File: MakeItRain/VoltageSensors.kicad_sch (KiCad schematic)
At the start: 4 parts, among them IC5 OPA2340PA

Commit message: wip
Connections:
- no-connect marks 3 -> 0
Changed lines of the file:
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@@
   (junction (at 132.08 77.47) (diameter 0) (color 0 0 0 0)
   )
-  (no_connect (at 163.83 80.01))
-  (no_connect (at 163.83 85.09))
-  (no_connect (at 163.83 82.55))
   (wire (pts (xy 119.38 81.28) (xy 119.38 82.55))
     (stroke (width 0) (type default) (color 0 0 0 0))

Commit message: wip for input fix.
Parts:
- R21: renamed from R5; footprint Resistor_THT:R_Axial_DIN0207_L6.3mm_D2.5mm_P5.08mm_Vertical -> Resistor_THT:R_Axial_DIN0207_L6.3mm_D2.5mm_P2.54mm_Vertical
- R22: renamed from R8; footprint Resistor_THT:R_Axial_DIN0207_L6.3mm_D2.5mm_P5.08mm_Vertical -> Resistor_THT:R_Axial_DIN0207_L6.3mm_D2.5mm_P2.54mm_Vertical
- R23: renamed from R13; footprint Resistor_THT:R_Axial_DIN0207_L6.3mm_D2.5mm_P5.08mm_Vertical -> Resistor_THT:R_Axial_DIN0207_L6.3mm_D2.5mm_P2.54mm_Vertical
- renumbered IC5 to IC3
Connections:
- net D36: now reaches IC3.1 (OUTA), IC3.2 (-INA), R23.1
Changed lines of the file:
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@@
+    (stroke (width 0) (type default) (color 0 0 0 0))
+  )
+  (wire (pts (xy 128.27 72.39) (xy 128.27 77.47))
     (stroke (width 0) (type default) (color 0 0 0 0))
   )
@@
     (stroke (width 0) (type default) (color 0 0 0 0))
   )
+  (global_label "D34" (shape input) (at 180.34 81.28 0) (fields_autoplaced)
+    (effects (font (size 1.27 1.27)) (justify left))
+    (property "Intersheet References" "${INTERSHEET_REFS}" (id 0) (at 186.3532 81.2006 0)
+      (effects (font (size 1.27 1.27)) (justify left) hide)
+    )
+  )
+  (global_label "D36" (shape input) (at 128.27 72.39 180) (fields_autoplaced)
+    (effects (font (size 1.27 1.27)) (justify right))
+    (property "Intersheet References" "${INTERSHEET_REFS}" (id 0) (at 122.2568 72.3106 0)
+      (effects (font (size 1.27 1.27)) (justify right) hide)
+    )
+  )
   (symbol (lib_id "Device:R") (at 119.38 77.47 0) (unit 1)
     (in_bom yes) (on_board yes)
-    (property "Reference" "R5" (id 0) (at 121.158 76.3016 0)
+    (property "Reference" "R21" (id 0) (at 121.158 76.3016 0)
       (effects (font (size 1.27 1.27)) (justify left))
     )
@@
       (effects (font (size 1.27 1.27)) (justify left))
     )
-    (property "Footprint" "Resistor_THT:R_Axial_DIN0207_L6.3mm_D2.5mm_P5.08mm_Vertical" (id 2) (at 117.602 77.47 90)
+    (property "Footprint" "Resistor_THT:R_Axial_DIN0207_L6.3mm_D2.5mm_P2.54mm_Vertical" (id 2) (at 117.602 77.47 90)
       (effects (font (size 1.27 1.27)) hide)
     )
@@
   (symbol (lib_id "power:+VDC") (at 119.38 68.58 0) (unit 1)
     (in_bom yes) (on_board yes)
-    (property "Reference" "#PWR027" (id 0) (at 119.38 71.12 0)
+    (property "Reference" "#PWR039" (id 0) (at 119.38 71.12 0)
       (effects (font (size 1.27 1.27)) hide)
     )
@@
   (symbol (lib_id "Device:R") (at 132.08 73.66 0) (mirror x) (unit 1)
     (in_bom yes) (on_board yes)
-    (property "Reference" "R13" (id 0) (at 133.858 74.8284 0)
+    (property "Reference" "R23" (id 0) (at 133.858 74.8284 0)
       (effects (font (size 1.27 1.27)) (justify left))
     )
@@
       (effects (font (size 1.27 1.27)) (justify left))
     )
-    (property "Footprint" "Resistor_THT:R_Axial_DIN0207_L6.3mm_D2.5mm_P5.08mm_Vertical" (id 2) (at 130.302 73.66 90)
+    (property "Footprint" "Resistor_THT:R_Axial_DIN0207_L6.3mm_D2.5mm_P2.54mm_Vertical" (id 2) (at 130.302 73.66 90)
       (effects (font (size 1.27 1.27)) hide)
     )
@@
   (symbol (lib_id "power:GND") (at 132.08 66.04 0) (mirror x) (unit 1)
     (in_bom yes) (on_board yes)
-    (property "Reference" "#PWR035" (id 0) (at 132.08 59.69 0)
+    (property "Reference" "#PWR041" (id 0) (at 132.08 59.69 0)
       (effects (font (size 1.27 1.27)) hide)
     )
@@
   (symbol (lib_id "power:GND") (at 119.38 95.25 0) (unit 1)
     (in_bom yes) (on_board yes)
-    (property "Reference" "#PWR031" (id 0) (at 119.38 101.6 0)
+    (property "Reference" "#PWR040" (id 0) (at 119.38 101.6 0)
       (effects (font (size 1.27 1.27)) hide)
     )
@@
   (symbol (lib_id "Device:R") (at 119.38 87.63 0) (unit 1)
     (in_bom yes) (on_board yes)
-    (property "Reference" "R8" (id 0) (at 121.158 86.4616 0)
+    (property "Reference" "R22" (id 0) (at 121.158 86.4616 0)
       (effects (font (size 1.27 1.27)) (justify left))
     )
@@
       (effects (font (size 1.27 1.27)) (justify left))
     )
-    (property "Footprint" "Resistor_THT:R_Axial_DIN0207_L6.3mm_D2.5mm_P5.08mm_Vertical" (id 2) (at 117.602 87.63 90)
+    (property "Footprint" "Resistor_THT:R_Axial_DIN0207_L6.3mm_D2.5mm_P2.54mm_Vertical" (id 2) (at 117.602 87.63 90)
       (effects (font (size 1.27 1.27)) hide)
     )
@@
   (symbol (lib_id "power:GND") (at 134.62 87.63 0) (unit 1)
     (in_bom yes) (on_board yes)
-    (property "Reference" "#PWR039" (id 0) (at 134.62 93.98 0)
+    (property "Reference" "#PWR042" (id 0) (at 134.62 93.98 0)
       (effects (font (size 1.27 1.27)) hide)
     )
@@
   (symbol (lib_id "SamacSys_Parts:OPA2340PA") (at 135.89 77.47 0) (unit 1)
     (in_bom yes) (on_board yes)
-    (property "Reference" "IC5" (id 0) (at 149.86 70.739 0))
+    (property "Reference" "IC3" (id 0) (at 149.86 70.739 0))
     (property "Value" "OPA2340PA" (id 1) (at 149.86 73.0504 0))
     (property "Footprint" "SamacSys_Parts:DIP794W53P254L959H508Q8N" (id 2) (at 160.02 74.93 0)

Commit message: wip for layout
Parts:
- added J4: Conn_01x03, Connector_PinHeader_2.54mm:PinHeader_1x03_P2.54mm_Vertical, symbol Connector_Generic:Conn_01x03
- added R?: 47k, Resistor_THT:R_Axial_DIN0207_L6.3mm_D2.5mm_P2.54mm_Vertical, symbol Device:R
- added RV1: 500k, Potentiometer_THT:Potentiometer_Bourns_3296W_Vertical, symbol Device:R_POT_US
- renumbered R21 to R23, R22 to R24, R23 to R25
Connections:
- net D34: now also IC3.6 (-INB), IC3.7 (OUTB), R?.1
- net GND: now also R?.2, RV1.3
- net at IC3.5 (+INB): now also J4.1 (Pin_1)
- new net: J4.2 (Pin_2), RV1.2
- new net: J4.3 (Pin_3), RV1.1
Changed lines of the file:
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@@
   (junction (at 132.08 77.47) (diameter 0) (color 0 0 0 0)
   )
+  (junction (at 172.72 80.01) (diameter 0) (color 0 0 0 0)
+  )
+  (junction (at 167.64 80.01) (diameter 0) (color 0 0 0 0)
+  )
   (wire (pts (xy 119.38 81.28) (xy 119.38 82.55))
     (stroke (width 0) (type default) (color 0 0 0 0))
   )
+  (wire (pts (xy 172.72 72.39) (xy 172.72 68.58))
+    (stroke (width 0) (type default) (color 0 0 0 0))
+  )
+  (wire (pts (xy 163.83 97.79) (xy 163.83 105.41))
+    (stroke (width 0) (type default) (color 0 0 0 0))
+  )
   (wire (pts (xy 134.62 85.09) (xy 135.89 85.09))
     (stroke (width 0) (type default) (color 0 0 0 0))
@@
     (stroke (width 0) (type default) (color 0 0 0 0))
   )
+  (wire (pts (xy 163.83 95.25) (xy 167.64 95.25))
+    (stroke (width 0) (type default) (color 0 0 0 0))
+  )
+  (wire (pts (xy 163.83 97.79) (xy 167.64 97.79))
+    (stroke (width 0) (type default) (color 0 0 0 0))
+  )
+  (wire (pts (xy 167.64 80.01) (xy 167.64 82.55))
+    (stroke (width 0) (type default) (color 0 0 0 0))
+  )
+  (wire (pts (xy 163.83 80.01) (xy 167.64 80.01))
+    (stroke (width 0) (type default) (color 0 0 0 0))
+  )
   (wire (pts (xy 163.83 77.47) (xy 167.64 77.47))
     (stroke (width 0) (type default) (color 0 0 0 0))
@@
     (stroke (width 0) (type default) (color 0 0 0 0))
   )
+  (wire (pts (xy 167.64 109.22) (xy 167.64 113.03))
+    (stroke (width 0) (type default) (color 0 0 0 0))
+  )
   (wire (pts (xy 128.27 72.39) (xy 128.27 77.47))
     (stroke (width 0) (type default) (color 0 0 0 0))
@@
     (stroke (width 0) (type default) (color 0 0 0 0))
   )
+  (wire (pts (xy 167.64 82.55) (xy 163.83 82.55))
+    (stroke (width 0) (type default) (color 0 0 0 0))
+  )
   (wire (pts (xy 134.62 87.63) (xy 134.62 85.09))
     (stroke (width 0) (type default) (color 0 0 0 0))
@@
     (stroke (width 0) (type default) (color 0 0 0 0))
   )
+  (wire (pts (xy 167.64 80.01) (xy 172.72 80.01))
+    (stroke (width 0) (type default) (color 0 0 0 0))
+  )
+  (wire (pts (xy 167.64 100.33) (xy 167.64 101.6))
+    (stroke (width 0) (type default) (color 0 0 0 0))
+  )
   (wire (pts (xy 119.38 82.55) (xy 119.38 83.82))
     (stroke (width 0) (type default) (color 0 0 0 0))
@@
     (stroke (width 0) (type default) (color 0 0 0 0))
   )
+  (wire (pts (xy 172.72 80.01) (xy 175.895 80.01))
+    (stroke (width 0) (type default) (color 0 0 0 0))
+  )
   (wire (pts (xy 132.08 69.85) (xy 132.08 66.04))
     (stroke (width 0) (type default) (color 0 0 0 0))
   )
-  (global_label "D34" (shape input) (at 180.34 81.28 0) (fields_autoplaced)
+  (wire (pts (xy 163.83 95.25) (xy 163.83 85.09))
+    (stroke (width 0) (type default) (color 0 0 0 0))
+  )
+  (global_label "D34" (shape input) (at 175.895 80.01 0) (fields_autoplaced)
     (effects (font (size 1.27 1.27)) (justify left))
-    (property "Intersheet References" "${INTERSHEET_REFS}" (id 0) (at 186.3532 81.2006 0)
+    (property "Intersheet References" "${INTERSHEET_REFS}" (id 0) (at 181.9082 79.9306 0)
       (effects (font (size 1.27 1.27)) (justify left) hide)
     )
@@
   (symbol (lib_id "Device:R") (at 119.38 77.47 0) (unit 1)
     (in_bom yes) (on_board yes)
-    (property "Reference" "R21" (id 0) (at 121.158 76.3016 0)
+    (property "Reference" "R23" (id 0) (at 121.158 76.3016 0)
       (effects (font (size 1.27 1.27)) (justify left))
     )
@@
   (symbol (lib_id "power:+VDC") (at 119.38 68.58 0) (unit 1)
     (in_bom yes) (on_board yes)
-    (property "Reference" "#PWR039" (id 0) (at 119.38 71.12 0)
+    (property "Reference" "#PWR042" (id 0) (at 119.38 71.12 0)
       (effects (font (size 1.27 1.27)) hide)
     )
@@
   (symbol (lib_id "Device:R") (at 132.08 73.66 0) (mirror x) (unit 1)
     (in_bom yes) (on_board yes)
-    (property "Reference" "R23" (id 0) (at 133.858 74.8284 0)
+    (property "Reference" "R25" (id 0) (at 133.858 74.8284 0)
       (effects (font (size 1.27 1.27)) (justify left))
     )
@@
   (symbol (lib_id "power:GND") (at 132.08 66.04 0) (mirror x) (unit 1)
     (in_bom yes) (on_board yes)
-    (property "Reference" "#PWR041" (id 0) (at 132.08 59.69 0)
+    (property "Reference" "#PWR044" (id 0) (at 132.08 59.69 0)
       (effects (font (size 1.27 1.27)) hide)
     )
@@
   (symbol (lib_id "power:GND") (at 119.38 95.25 0) (unit 1)
     (in_bom yes) (on_board yes)
-    (property "Reference" "#PWR040" (id 0) (at 119.38 101.6 0)
+    (property "Reference" "#PWR043" (id 0) (at 119.38 101.6 0)
       (effects (font (size 1.27 1.27)) hide)
     )
@@
     (pin "1")
   )
+  (symbol (lib_id "power:GND") (at 172.72 68.58 0) (mirror x) (unit 1)
+    (in_bom yes) (on_board yes)
+    (property "Reference" "#PWR?" (id 0) (at 172.72 62.23 0)
+      (effects (font (size 1.27 1.27)) hide)
+    )
+    (property "Value" "GND" (id 1) (at 172.847 64.1858 0))
+    (property "Footprint" "" (id 2) (at 172.72 68.58 0)
+      (effects (font (size 1.27 1.27)) hide)
+    )
+    (property "Datasheet" "" (id 3) (at 172.72 68.58 0)
+      (effects (font (size 1.27 1.27)) hide)
+    )
+    (pin "1")
+  )
+  (symbol (lib_id "Connector_Generic:Conn_01x03") (at 172.72 97.79 0) (unit 1)
+    (in_bom yes) (on_board yes) (fields_autoplaced)
+    (property "Reference" "J4" (id 0) (at 174.752 96.8815 0)
+      (effects (font (size 1.27 1.27)) (justify left))
+    )
+    (property "Value" "Conn_01x03" (id 1) (at 174.752 99.6566 0)
+      (effects (font (size 1.27 1.27)) (justify left))
+    )
+    (property "Footprint" "Connector_PinHeader_2.54mm:PinHeader_1x03_P2.54mm_Vertical" (id 2) (at 172.72 97.79 0)
+      (effects (font (size 1.27 1.27)) hide)
+    )
+    (property "Datasheet" "~" (id 3) (at 172.72 97.79 0)
+      (effects (font (size 1.27 1.27)) hide)
+    )
+    (pin "1")
+    (pin "2")
+    (pin "3")
+  )
+  (symbol (lib_id "Device:R_POT_US") (at 167.64 105.41 0) (mirror y) (unit 1)
+    (in_bom yes) (on_board yes)
+    (property "Reference" "RV1" (id 0) (at 169.3672 104.2416 0)
+      (effects (font (size 1.27 1.27)) (justify right))
+    )
+    (property "Value" "500k" (id 1) (at 169.3672 106.553 0)
+      (effects (font (size 1.27 1.27)) (justify right))
+    )
+    (property "Footprint" "Potentiometer_THT:Potentiometer_Bourns_3296W_Vertical" (id 2) (at 167.64 105.41 0)
+      (effects (font (size 1.27 1.27)) hide)
+    )
+    (property "Datasheet" "~" (id 3) (at 167.64 105.41 0)
+      (effects (font (size 1.27 1.27)) hide)
+    )
+    (pin "1")
+    (pin "2")
+    (pin "3")
+  )
   (symbol (lib_id "power:+3.3V") (at 167.64 74.93 0) (unit 1)
     (in_bom yes) (on_board yes)
-    (property "Reference" "#PWR043" (id 0) (at 167.64 78.74 0)
+    (property "Reference" "#PWR046" (id 0) (at 167.64 78.74 0)
       (effects (font (size 1.27 1.27)) hide)
     )
@@
   (symbol (lib_id "Device:R") (at 119.38 87.63 0) (unit 1)
     (in_bom yes) (on_board yes)
-    (property "Reference" "R22" (id 0) (at 121.158 86.4616 0)
+    (property "Reference" "R24" (id 0) (at 121.158 86.4616 0)
       (effects (font (size 1.27 1.27)) (justify left))
     )
@@
     (pin "2")
   )
+  (symbol (lib_id "Device:R") (at 172.72 76.2 0) (mirror x) (unit 1)
+    (in_bom yes) (on_board yes)
+    (property "Reference" "R?" (id 0) (at 174.498 77.3684 0)
+      (effects (font (size 1.27 1.27)) (justify left))
+    )
+    (property "Value" "47k" (id 1) (at 174.498 75.057 0)
+      (effects (font (size 1.27 1.27)) (justify left))
+    )
+    (property "Footprint" "Resistor_THT:R_Axial_DIN0207_L6.3mm_D2.5mm_P2.54mm_Vertical" (id 2) (at 170.942 76.2 90)
+      (effects (font (size 1.27 1.27)) hide)
+    )
+    (property "Datasheet" "~" (id 3) (at 172.72 76.2 0)
+      (effects (font (size 1.27 1.27)) hide)
+    )
+    (pin "1")
+    (pin "2")
+  )
+  (symbol (lib_id "power:GND") (at 167.64 113.03 0) (mirror y) (unit 1)
+    (in_bom yes) (on_board yes)
+    (property "Reference" "#PWR047" (id 0) (at 167.64 119.38 0)
+      (effects (font (size 1.27 1.27)) hide)
+    )
+    (property "Value" "GND" (id 1) (at 167.64 116.84 0))
+    (property "Footprint" "" (id 2) (at 167.64 113.03 0))
+    (property "Datasheet" "" (id 3) (at 167.64 113.03 0))
+    (pin "1")
+  )
   (symbol (lib_id "power:GND") (at 134.62 87.63 0) (unit 1)
     (in_bom yes) (on_board yes)
-    (property "Reference" "#PWR042" (id 0) (at 134.62 93.98 0)
-      (effects (font (size 1.27 1.27)) hide)
-    )
+    (property "Reference" "#PWR045" (id 0) (at 134.62 93.98 0)
+      (effects (font (size 1.27 1.27)) hide)
+    )

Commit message: pre routing
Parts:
- removed J4: Conn_01x03, Connector_PinHeader_2.54mm:PinHeader_1x03_P2.54mm_Vertical, symbol Connector_Generic:Conn_01x03
- added J4: Conn_01x01, Connector_PinHeader_2.54mm:PinHeader_1x01_P2.54mm_Vertical, symbol Connector_Generic:Conn_01x01
- gave numbers to parts that had none: 1
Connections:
- net at IC3.5 (+INB): now also RV1.2
- net AuxVoltage: now reaches RV1.1
- net AuxVoltage: now also J4.1 (Pin_1)
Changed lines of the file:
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@@
-    (stroke (width 0) (type default) (color 0 0 0 0))
-  )
-  (wire (pts (xy 163.83 97.79) (xy 163.83 105.41))
     (stroke (width 0) (type default) (color 0 0 0 0))
   )
@@
     (stroke (width 0) (type default) (color 0 0 0 0))
   )
-  (wire (pts (xy 163.83 95.25) (xy 167.64 95.25))
-    (stroke (width 0) (type default) (color 0 0 0 0))
-  )
-  (wire (pts (xy 163.83 97.79) (xy 167.64 97.79))
-    (stroke (width 0) (type default) (color 0 0 0 0))
-  )
   (wire (pts (xy 167.64 80.01) (xy 167.64 82.55))
     (stroke (width 0) (type default) (color 0 0 0 0))
@@
     (stroke (width 0) (type default) (color 0 0 0 0))
   )
+  (wire (pts (xy 167.64 100.33) (xy 167.64 101.6))
+    (stroke (width 0) (type default) (color 0 0 0 0))
+  )
   (wire (pts (xy 163.83 77.47) (xy 167.64 77.47))
     (stroke (width 0) (type default) (color 0 0 0 0))
@@
     (stroke (width 0) (type default) (color 0 0 0 0))
   )
-  (wire (pts (xy 167.64 100.33) (xy 167.64 101.6))
+  (wire (pts (xy 180.975 100.33) (xy 167.64 100.33))
     (stroke (width 0) (type default) (color 0 0 0 0))
   )
@@
     (stroke (width 0) (type default) (color 0 0 0 0))
   )
-  (wire (pts (xy 163.83 95.25) (xy 163.83 85.09))
-    (stroke (width 0) (type default) (color 0 0 0 0))
+  (wire (pts (xy 163.83 85.09) (xy 163.83 105.41))
+    (stroke (width 0) (type default) (color 0 0 0 0))
+  )
+  (global_label "AuxVoltage" (shape input) (at 175.895 100.33 270) (fields_autoplaced)
+    (effects (font (size 1.27 1.27)) (justify right))
+    (property "Intersheet References" "${INTERSHEET_REFS}" (id 0) (at 175.9744 112.9352 90)
+      (effects (font (size 1.27 1.27)) (justify left) hide)
+    )
   )
   (global_label "D34" (shape input) (at 175.895 80.01 0) (fields_autoplaced)
@@
   (symbol (lib_id "power:GND") (at 172.72 68.58 0) (mirror x) (unit 1)
     (in_bom yes) (on_board yes)
-    (property "Reference" "#PWR?" (id 0) (at 172.72 62.23 0)
+    (property "Reference" "#PWR0101" (id 0) (at 172.72 62.23 0)
       (effects (font (size 1.27 1.27)) hide)
     )
@@
     (pin "1")
   )
-  (symbol (lib_id "Connector_Generic:Conn_01x03") (at 172.72 97.79 0) (unit 1)
-    (in_bom yes) (on_board yes) (fields_autoplaced)
-    (property "Reference" "J4" (id 0) (at 174.752 96.8815 0)
-      (effects (font (size 1.27 1.27)) (justify left))
-    )
-    (property "Value" "Conn_01x03" (id 1) (at 174.752 99.6566 0)
-      (effects (font (size 1.27 1.27)) (justify left))
-    )
-    (property "Footprint" "Connector_PinHeader_2.54mm:PinHeader_1x03_P2.54mm_Vertical" (id 2) (at 172.72 97.79 0)
-      (effects (font (size 1.27 1.27)) hide)
-    )
-    (property "Datasheet" "~" (id 3) (at 172.72 97.79 0)
-      (effects (font (size 1.27 1.27)) hide)
-    )
-    (pin "1")
-    (pin "2")
-    (pin "3")
-  )
   (symbol (lib_id "Device:R_POT_US") (at 167.64 105.41 0) (mirror y) (unit 1)
     (in_bom yes) (on_board yes)
@@
   (symbol (lib_id "Device:R") (at 172.72 76.2 0) (mirror x) (unit 1)
     (in_bom yes) (on_board yes)
-    (property "Reference" "R?" (id 0) (at 174.498 77.3684 0)
+    (property "Reference" "R34" (id 0) (at 174.498 77.3684 0)
       (effects (font (size 1.27 1.27)) (justify left))
     )
@@
     (pin "8")
   )
+  (symbol (lib_id "Connector_Generic:Conn_01x01") (at 186.055 100.33 0) (unit 1)
+    (in_bom yes) (on_board yes) (fields_autoplaced)
+    (property "Reference" "J4" (id 0) (at 188.087 99.4215 0)
+      (effects (font (size 1.27 1.27)) (justify left))
+    )
+    (property "Value" "Conn_01x01" (id 1) (at 188.087 102.1966 0)
+      (effects (font (size 1.27 1.27)) (justify left))
+    )
+    (property "Footprint" "Connector_PinHeader_2.54mm:PinHeader_1x01_P2.54mm_Vertical" (id 2) (at 186.055 100.33 0)
+      (effects (font (size 1.27 1.27)) hide)
+    )
+    (property "Datasheet" "~" (id 3) (at 186.055 100.33 0)
+      (effects (font (size 1.27 1.27)) hide)
+    )
+    (pin "1")
+  )
 )

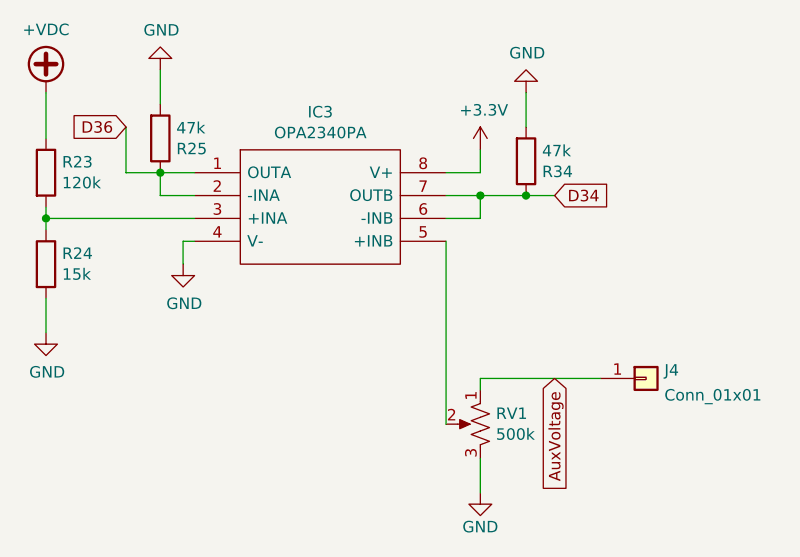
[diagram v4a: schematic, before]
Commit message: working on pin reassignment to fix the stupid stupid ways that esp32 are designed in hardware that require much in way of digging through docs cause not all gpio are created equal.
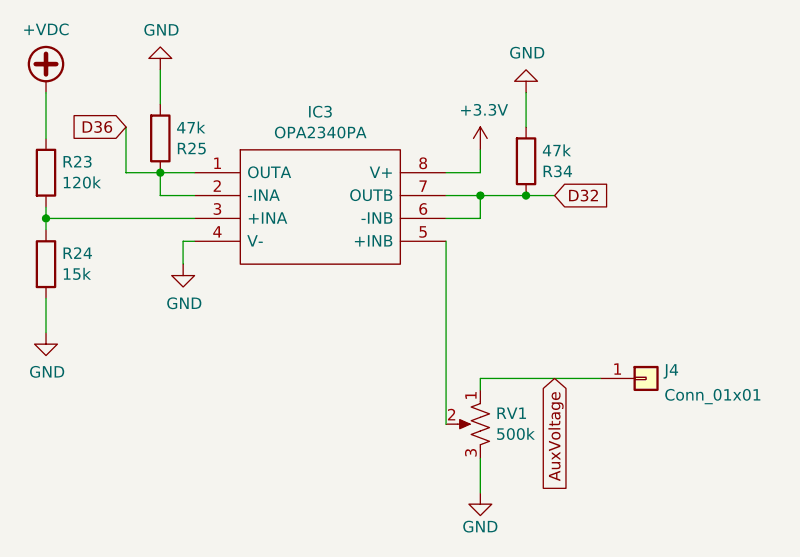
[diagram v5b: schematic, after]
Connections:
- net D34 renamed D32
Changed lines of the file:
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@@
     )
   )
-  (global_label "D34" (shape input) (at 175.895 80.01 0) (fields_autoplaced)
+  (global_label "D32" (shape input) (at 175.895 80.01 0) (fields_autoplaced)
     (effects (font (size 1.27 1.27)) (justify left))
     (property "Intersheet References" "${INTERSHEET_REFS}" (id 0) (at 181.9082 79.9306 0)

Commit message: i think i have the pins finally figured out. Need to breadboard this setup to make sure it works.
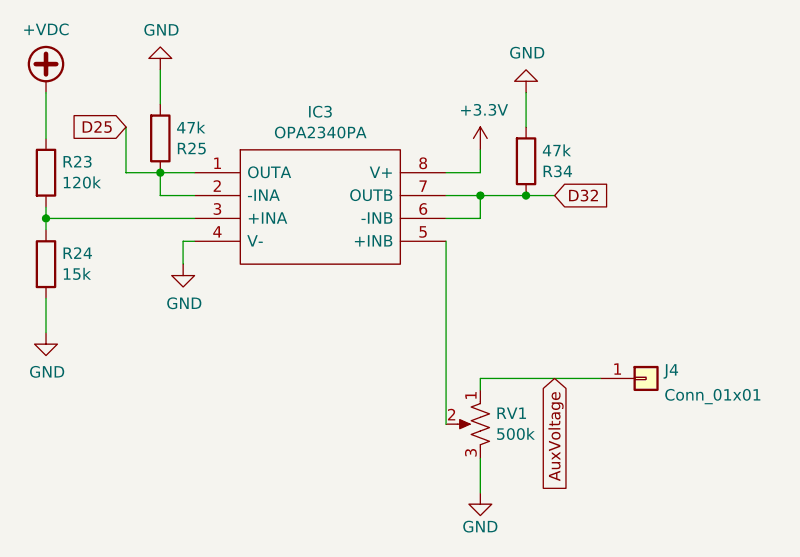
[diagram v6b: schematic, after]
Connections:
- net D36 renamed D25
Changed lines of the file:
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@@
     )
   )
-  (global_label "D36" (shape input) (at 128.27 72.39 180) (fields_autoplaced)
+  (global_label "D25" (shape input) (at 128.27 72.39 180) (fields_autoplaced)
     (effects (font (size 1.27 1.27)) (justify right))
     (property "Intersheet References" "${INTERSHEET_REFS}" (id 0) (at 122.2568 72.3106 0)
